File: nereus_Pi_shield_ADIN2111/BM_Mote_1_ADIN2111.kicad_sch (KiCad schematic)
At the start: 31 parts, among them U1 ADIN2111BCPZ, U2 AP22913CN4-7, U3 AP22913CN4-7, Y1 ABM11W-25.0000MHZ-6-K1Z-T3

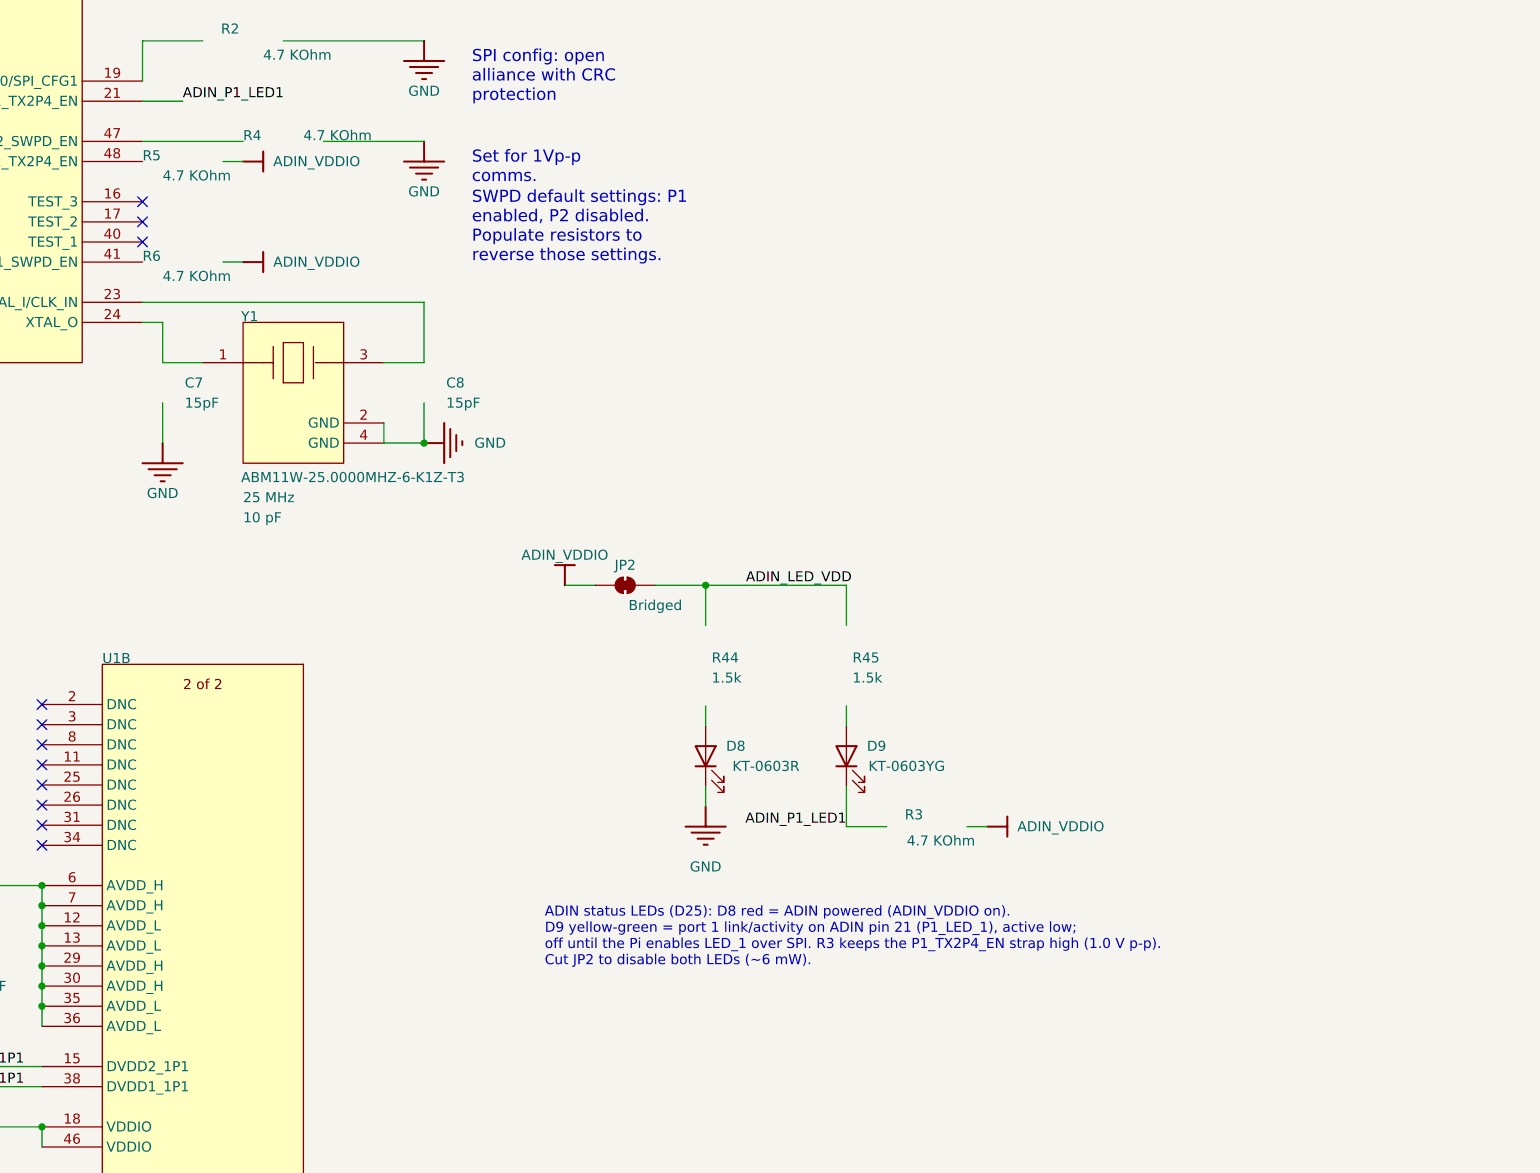
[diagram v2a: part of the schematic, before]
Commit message: S5.f: port-2 status LED D10 (ADIN pin 48, R46 1.5k, R5 as pull-up) at Nick's request
R5 redrawn into the LED group like R3 (connections unchanged), U1 pin 48 stub +
label ADIN_P2_LED1; D10 branch on the ADIN_LED_VDD wire; note reflowed. ERC
27/504; netcheck 51/51.

Co-Authored-By: Claude Opus 5.5 <noreply@anthropic.com>
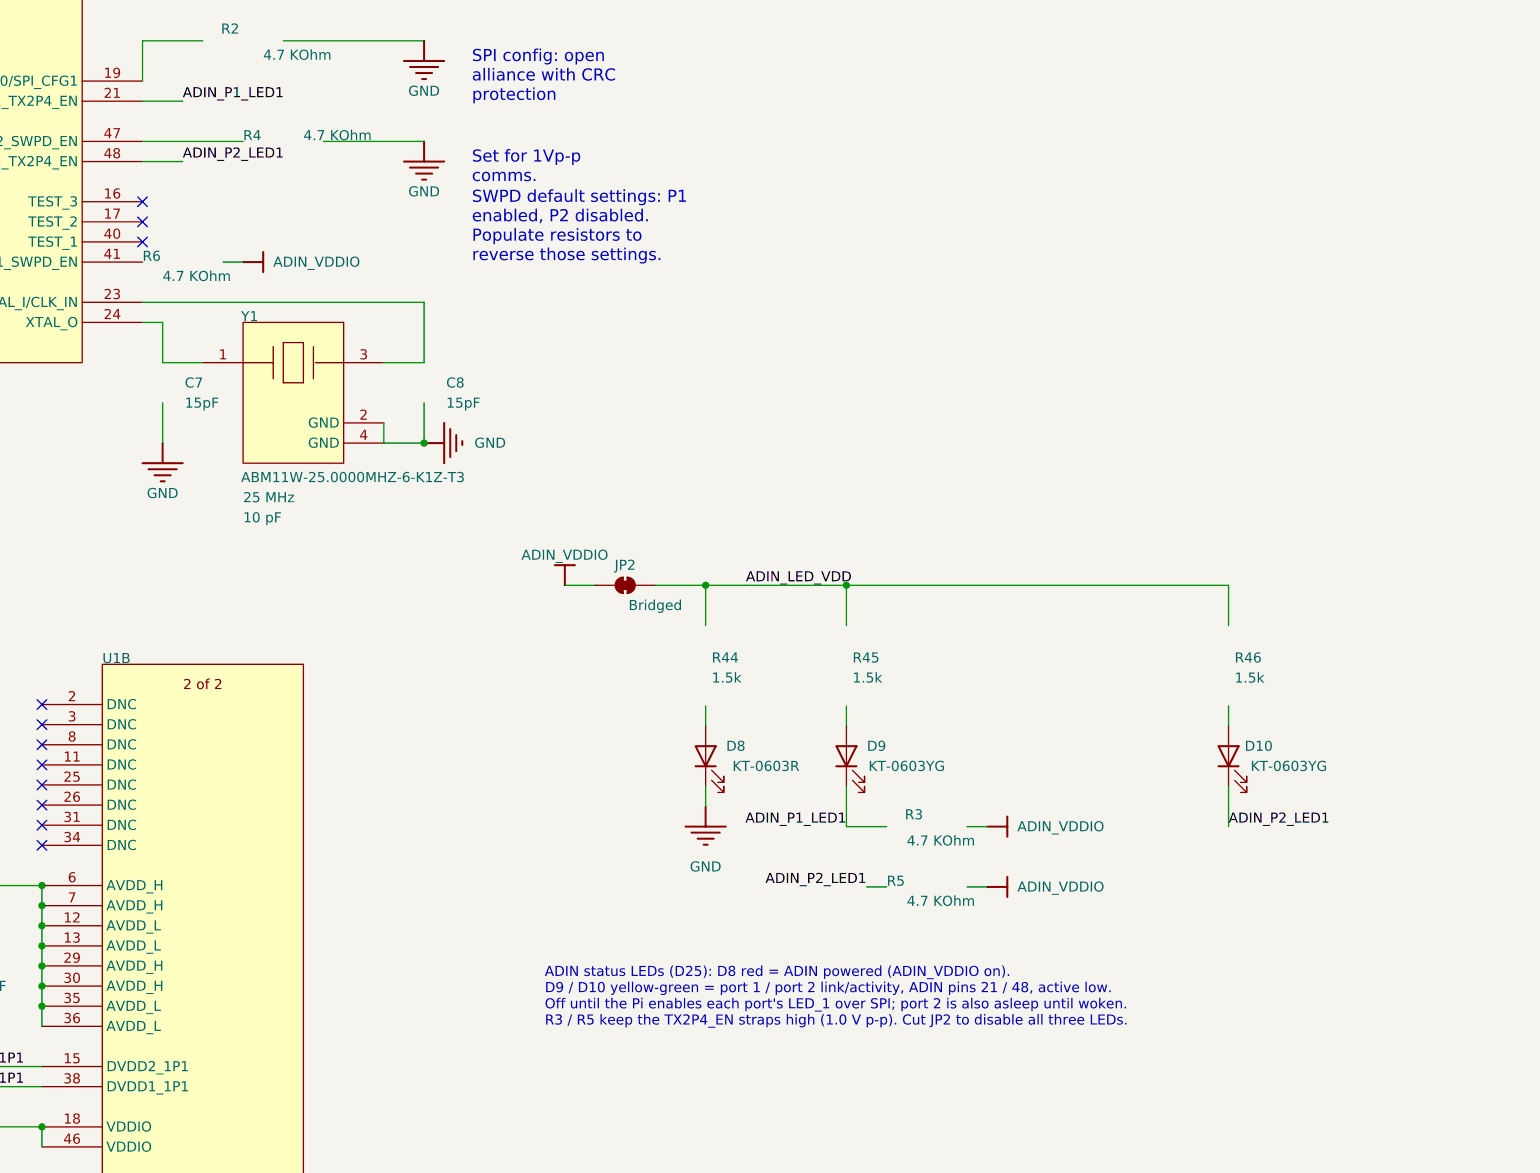
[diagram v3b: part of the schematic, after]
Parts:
- added D10: KT-0603YG, LED_SMD:LED_0603_1608Metric, symbol Device:LED
- added R46: RC0402FR-071K5L, Vault:RESC1005X40X25ML05T10, symbol BM_Mote_000639-AB-altium-import:ADIN_1_RES_Altium Content Vault_0
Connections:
- net ADIN_P2_LED1: now reaches U1.48 (P2_LED_1/P2_TX2P4_EN)
- net ADIN_P2_LED1: now also D10.1 (K)
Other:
- note added: "ADIN status LEDs (D25): D8 red = ADIN powered (ADIN_VDDIO on). D9 / D10 yellow-green = port 1 / port 2 link/activity, ADIN pins 21 / 48, active low. Off until the Pi enables each port's LED_1 over SPI; port 2 is also asleep until woken. R3 / R5 keep the TX2P4_EN straps high (1.0 V p-p). Cut JP2 to disable all three LEDs."
- note removed: "ADIN status LEDs (D25): D8 red = ADIN powered (ADIN_VDDIO on). D9 yellow-green = port 1 link/activity on ADIN pin 21 (P1_LED_1), active low; off until the Pi enables LED_1 over SPI. R3 keeps the P1_TX2P4_EN strap high (1.0 V p-p). Cut JP2 to disable both LEDs (~6 mW)."

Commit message: S5.h: BOM alternates as hidden ALT/SOURCING fields; tracked bom.csv
- 24 flagged passives: hidden ALT1/ALT2 MPN/MFR/LCSC, ALT NOTE, SOURCING
  (values from docs/design-review/bom_alternates.md, D26)
- Critical parts (U1-U3, L3/L6, Y1, D1-D3, MP1-MP4, J5, J1): SOURCING only
- tools/check.sh exports docs/design-review/bom.csv: specified part first,
  alternates beside it; grouped by Value + DNP (R11 apart from R12/R13/R17/R19)
- J1 Footprint property re-indented (whitespace; import leftover)
- Fields only: ERC 531/27/504 unchanged, netcheck 51/51, midwire 0;
  netlist diff = the 208 new fields
- Docs: bom_alternates, bom_lifecycle, sofar_brief, changelog, DESIGN,
  TRACKER, viewer, DEV_LOG

Co-Authored-By: Claude Opus 5.5 <noreply@anthropic.com>
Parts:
- U1: SOURCING (none) -> JLC global sourcing (D26); no LCSC listing, DK 120
- U2, U3: SOURCING (none) -> JLC global sourcing, all 40 (LCSC has 30) (D26)
- Y1: SOURCING (none) -> JLC global sourcing (D26); no LCSC listing, DK 87
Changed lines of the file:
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@@
 			)
 		)
+		(property "SOURCING" "JLC global sourcing (D26); no LCSC listing, DK 120"
+			(at 259.08 203.0222 0)
+			(effects
+				(font
+					(size 1.27 1.27)
+				)
+				(hide yes)
+			)
+		)
 		(pin "2"
 		)
@@
 			)
 		)
+		(property "SOURCING" "JLC global sourcing, all 40 (LCSC has 30) (D26)"
+			(at 177.8 228.4222 0)
+			(effects
+				(font
+					(size 1.27 1.27)
+				)
+				(hide yes)
+			)
+		)
 		(pin "A1"
 		)
@@
 			)
 		)
+		(property "SOURCING" "JLC global sourcing, all 40 (LCSC has 30) (D26)"
+			(at 177.8 197.9422 0)
+			(effects
+				(font
+					(size 1.27 1.27)
+				)
+				(hide yes)
+			)
+		)
 		(pin "A1"
 		)
@@
 			)
 		)
+		(property "SOURCING" "JLC global sourcing (D26); no LCSC listing, DK 120"
+			(at 205.74 98.8822 0)
+			(effects
+				(font
+					(size 1.27 1.27)
+				)
+				(hide yes)
+			)
+		)
 		(pin "48"
 		)
@@
 				(hide yes)
 			)
+		)
+		(property "SOURCING" "JLC global sourcing (D26); no LCSC listing, DK 87"
+			(at 259.08 131.9022 0)
+			(effects
+				(font
+					(size 1.27 1.27)
+				)
+				(hide yes)
+			)

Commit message: S5.i: planned part per BOM line (D27) beside Sofar's specified part
- PLANNED MPN/MFR/LCSC + PLANNED NOTE (why) on all 106 purchased parts;
  Value (Sofar's part) unchanged
- 10 lines planned as LCSC-stocked equivalents (R34, R20/R39, R21 group,
  C31, C17/C26, C21, C16 group, C19/C27, R14/R18) and D1 -> Sofar's Vishay
  second source; R8 kept (no ROHM land pattern); J1 TBD; rest as specified
- SOURCING on the 19 changed-line parts: planned part after Sofar approves
- Footprint lines of U11, R41, C56-C58 re-indented (whitespace only)
- View "Sofar review (planned parts)"; check.sh exports bom.csv from it
- Fields only: ERC 531/27/504 unchanged, netcheck 51/51, midwire 0
- Docs: DESIGN D27, bom_alternates, bom_lifecycle, sofar_brief, changelog,
  TRACKER, viewer, DEV_LOG

Co-Authored-By: Claude Opus 5.5 <noreply@anthropic.com>
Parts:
- C1, C10, C11, C12, C13, C14, C3, C9: PLANNED LCSC (none) -> C100072; PLANNED MFR (none) -> Samsung; PLANNED MPN (none) -> CL05A104KA5NNNC; PLANNED NOTE (none) -> As specified; in LCSC stock (checked 2026-10-06)
- C2, C4: PLANNED LCSC (none) -> C14445; PLANNED MFR (none) -> Samsung; PLANNED MPN (none) -> CL05A105KP5NNNC; PLANNED NOTE (none) -> As specified; in LCSC stock (checked 2026-10-06)
- C5, C6: PLANNED LCSC (none) -> C113784; PLANNED MFR (none) -> Yageo; PLANNED MPN (none) -> CC0402KRX5R6BB684; PLANNED NOTE (none) -> As specified; in LCSC stock (checked 2026-10-06)
- C7, C8: PLANNED LCSC (none) -> C106997; PLANNED MFR (none) -> Yageo; PLANNED MPN (none) -> CC0402JRNPO9BN150; PLANNED NOTE (none) -> As specified; in LCSC stock (checked 2026-10-06)
- D10, D9: PLANNED LCSC (none) -> C2289; PLANNED MFR (none) -> Hubei KENTO; PLANNED MPN (none) -> KT-0603YG; PLANNED NOTE (none) -> As specified; in LCSC stock (checked 2026-10-06)
- D8: PLANNED LCSC (none) -> C2286; PLANNED MFR (none) -> Hubei KENTO; PLANNED MPN (none) -> KT-0603R; PLANNED NOTE (none) -> As specified; in LCSC stock (checked 2026-10-06)
- R1, R44, R45, R46: PLANNED LCSC (none) -> C114759; PLANNED MFR (none) -> Yageo; PLANNED MPN (none) -> RC0402FR-071K5L; PLANNED NOTE (none) -> As specified; in LCSC stock (checked 2026-10-06)
- R2, R3, R4, R5, R6: PLANNED LCSC (none) -> C400631; PLANNED MFR (none) -> Panasonic; PLANNED MPN (none) -> ERJ-2RKF4701X; PLANNED NOTE (none) -> As specified; in LCSC stock (checked 2026-10-06)
- U1: PLANNED MFR (none) -> Analog Devices; PLANNED MPN (none) -> ADIN2111BCPZ; PLANNED NOTE (none) -> As specified; JLC global sourcing (D26): no LCSC listing
- U2, U3: PLANNED LCSC (none) -> C2150198; PLANNED MFR (none) -> Diodes Inc.; PLANNED MPN (none) -> AP22913CN4-7; PLANNED NOTE (none) -> As specified; LCSC has 30 of the 40 needed (2026-10-06): JL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
- Y1: PLANNED MFR (none) -> Abracon; PLANNED MPN (none) -> ABM11W-25.0000MHZ-6-K1Z-T3; PLANNED NOTE (none) -> As specified; JLC global sourcing (D26): no LCSC listing

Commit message: S6.a: BOM hygiene -- TP/FID/MTG out of the BOM; MANUFACTURER filled
- in_bom no on TP x16, FID1-6, MTG1-4 (bare copper / holes)
- MANUFACTURER on the 75 BOM parts without one, from bom_lifecycle.md;
  Sofar's MFR_NAME / MANUFACTURER1 / MANUFACTURER 1 untouched; J1 open
- bom.csv 51 rows, Mfr on every row but J1
- ERC 531/27/504 unchanged, netcheck 51/51, midwire 0
- Docs: bom_lifecycle, changelog, DESIGN, TRACKER (S6 bites), viewer, DEV_LOG

Co-Authored-By: Claude Opus 5.5 <noreply@anthropic.com>
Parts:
- C1, C10, C11, C12, C13, C14, C2, C3, C4, C9: MANUFACTURER (none) -> Samsung
- C7, C8: MANUFACTURER (none) -> Yageo
- R2, R3, R4, R5, R6: MANUFACTURER (none) -> Panasonic
- TP1, TP2: now left out of the parts list
- U1: MANUFACTURER (none) -> Analog Devices
- U2, U3: MANUFACTURER (none) -> Diodes Inc.
- Y1: MANUFACTURER (none) -> Abracon
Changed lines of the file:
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@@
 		(unit 0)
 		(exclude_from_sim no)
-		(in_bom yes)
+		(in_bom no)
 		(on_board yes)
 		(dnp no)
@@
 			)
 		)
+		(property "MANUFACTURER" "Analog Devices"
+			(at 259.08 203.0222 0)
+			(effects
+				(font
+					(size 1.27 1.27)
+				)
+				(hide yes)
+			)
+		)
 		(pin "2"
 		)
@@
 			)
 		)
+		(property "MANUFACTURER" "Samsung"
+			(at 226.06 228.4222 0)
+			(effects
+				(font
+					(size 1.27 1.27)
+				)
+				(hide yes)
+			)
+		)
 		(pin "1"
 		)
@@
 		(unit 0)
 		(exclude_from_sim no)
-		(in_bom yes)
+		(in_bom no)
 		(on_board yes)
 		(dnp no)
@@
 			)
 		)
+		(property "MANUFACTURER" "Diodes Inc."
+			(at 177.8 228.4222 0)
+			(effects
+				(font
+					(size 1.27 1.27)
+				)
+				(hide yes)
+			)
+		)
 		(pin "A1"
 		)
@@
 			)
 		)
+		(property "MANUFACTURER" "Samsung"
+			(at 276.86 70.9422 0)
+			(effects
+				(font
+					(size 1.27 1.27)
+				)
+				(hide yes)
+			)
+		)
 		(pin "1"
 		)
@@
 			)
 		)
+		(property "MANUFACTURER" "Panasonic"
+			(at 347.98 198.12 0)
+			(effects
+				(font
+					(size 1.27 1.27)
+				)
+				(hide yes)
+			)
+		)
 		(pin "2"
 		)
@@
 			)
 		)
+		(property "MANUFACTURER" "Panasonic"
+			(at 261.62 91.2622 0)
+			(effects
+				(font
+					(size 1.27 1.27)
+				)
+				(hide yes)
+			)
+		)
 		(pin "2"
 		)
@@
 			)
 		)
+		(property "MANUFACTURER" "Samsung"
+			(at 226.06 200.4822 0)
+			(effects
+				(font
+					(size 1.27 1.27)
+				)
+				(hide yes)
+			)
+		)
 		(pin "1"
 		)
@@
 			)
 		)
+		(property "MANUFACTURER" "Diodes Inc."
+			(at 177.8 197.9422 0)
+			(effects
+				(font
+					(size 1.27 1.27)
+				)
+				(hide yes)
+			)
+		)
 		(pin "A1"
 		)
@@
 			)
 		)
+		(property "MANUFACTURER" "Yageo"
+			(at 254 131.9022 0)
+			(effects
+				(font
+					(size 1.27 1.27)
+				)
+				(hide yes)
+			)
+		)
 		(pin "1"
 		)
@@
 			)
 		)
+		(property "MANUFACTURER" "Analog Devices"
+			(at 205.74 98.8822 0)
+			(effects
+				(font
+					(size 1.27 1.27)
+				)
+				(hide yes)
+			)
+		)
 		(pin "48"
 		)
@@
 			)
 		)
+		(property "MANUFACTURER" "Yageo"
+			(at 287.02 131.9022 0)
+			(effects
+				(font
+					(size 1.27 1.27)
+				)
+				(hide yes)
+			)
+		)
 		(pin "1"
 		)
@@
 			)
 		)
+		(property "MANUFACTURER" "Abracon"
+			(at 259.08 131.9022 0)
+			(effects
+				(font
+					(size 1.27 1.27)
+				)
+				(hide yes)
+			)
+		)
 		(pin "1"
 		)
@@
 			)
 		)
+		(property "MANUFACTURER" "Panasonic"
+			(at 266.7 103.9622 0)
+			(effects
+				(font
+					(size 1.27 1.27)
+				)
+				(hide yes)
+			)
+		)
 		(pin "1"
 		)
@@
 			)
 		)
+		(property "MANUFACTURER" "Samsung"
+			(at 292.1 68.4022 0)
+			(effects
+				(font
+					(size 1.27 1.27)
+				)
+				(hide yes)
+			)
+		)
 		(pin "1"
 		)
@@
 			)
 		)
+		(property "MANUFACTURER" "Samsung"
+			(at 304.8 65.8622 0)
+			(effects
+				(font
+					(size 1.27 1.27)
+				)
+				(hide yes)
+			)
+		)
 		(pin "1"
 		)
@@
 			)
 		)
+		(property "MANUFACTURER" "Panasonic"
+			(at 347.98 190.5 0)
+			(effects
+				(font
+					(size 1.27 1.27)
+				)
+				(hide yes)
+			)
+		)
 		(pin "2"
 		)
@@
 			)
 		)
+		(property "MANUFACTURER" "Samsung"
+			(at 264.16 73.4822 0)
+			(effects
+				(font
+					(size 1.27 1.27)
+				)
+				(hide yes)
+			)
+		)
 		(pin "1"
 		)
@@
 			)
 		)
+		(property "MANUFACTURER" "Samsung"
+			(at 215.9 228.4222 0)
+			(effects
+				(font
+					(size 1.27 1.27)
+				)
+				(hide yes)
+			)
+		)
 		(pin "1"
 		)
@@
 			)
 		)
+		(property "MANUFACTURER" "Samsung"
+			(at 215.9 200.4822 0)
+			(effects
+				(font
+					(size 1.27 1.27)
+				)
+				(hide yes)
+			)
+		)
 		(pin "1"
 		)
@@
 			)
 		)
+		(property "MANUFACTURER" "Panasonic"
+			(at 254 119.2022 0)
+			(effects
+				(font
+					(size 1.27 1.27)
+				)
+				(hide yes)
+			)
+		)
 		(pin "2"
 		)
@@
 			)
 		)
+		(property "MANUFACTURER" "Samsung"
+			(at 193.04 200.4822 0)
+			(effects
+				(font
+					(size 1.27 1.27)
+				)
+				(hide yes)
+			)
+		)
 		(pin "1"
 		)
@@
 			(at 205.74 200.4822 0)
 			(effects
+				(font
+					(size 1.27 1.27)
+				)
+				(hide yes)
+			)
+		)
+		(property "MANUFACTURER" "Samsung"
+			(at 205.74 200.4822 0)
+			(effects
